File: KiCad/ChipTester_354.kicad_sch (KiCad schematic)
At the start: 3 parts

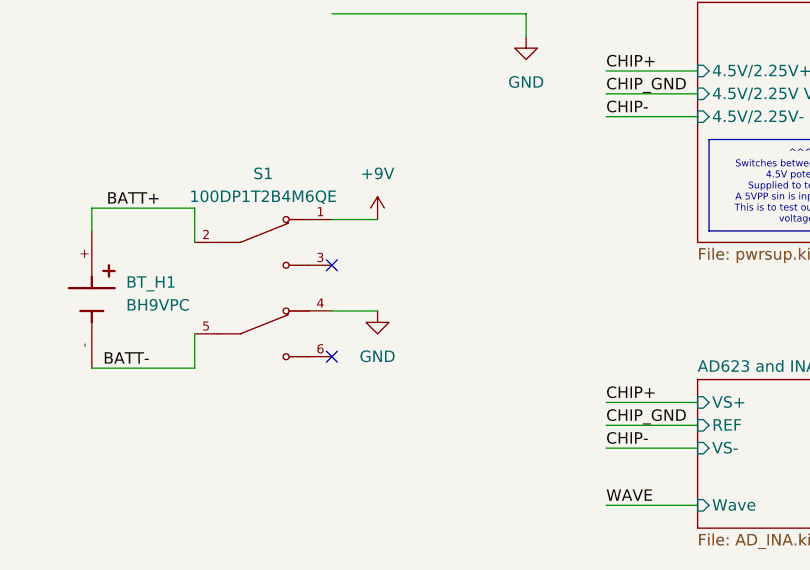
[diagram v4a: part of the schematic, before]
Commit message: Add power led
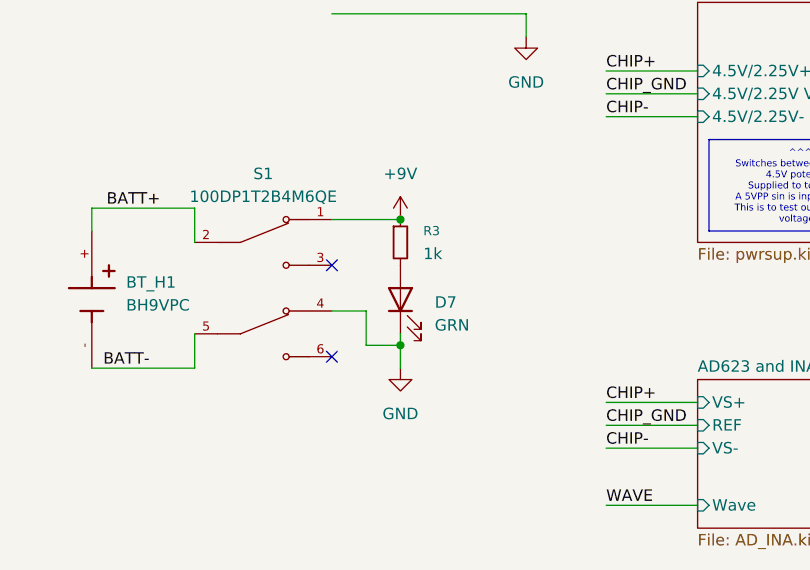
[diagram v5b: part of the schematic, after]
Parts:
- added D7: GRN, symbol Device:LED
- added R3: 1k, symbol Device:R_Small
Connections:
- net +9V: now also R3.1
- net GND: now also D7.1 (K)
- new net: D7.2 (A), R3.2
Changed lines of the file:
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@@
+	)
+	(junction
+		(at 111.76 54.61)
+		(diameter 0)
+		(color 0 0 0 0)
 	)
 	(junction
@@
 		(color 0 0 0 0)
 	)
+	(junction
+		(at 111.76 68.58)
+		(diameter 0)
+		(color 0 0 0 0)
+	)
 	(no_connect
 		(at 104.14 59.69)
@@
 	(wire
 		(pts
+			(xy 107.95 64.77) (xy 107.95 68.58)
+		)
+		(stroke
+			(width 0)
+			(type default)
+		)
+	)
+	(wire
+		(pts
 			(xy 217.17 40.64) (xy 227.33 40.64)
 		)
@@
 	(wire
 		(pts
+			(xy 111.76 68.58) (xy 111.76 67.31)
+		)
+		(stroke
+			(width 0)
+			(type default)
+		)
+	)
+	(wire
+		(pts
 			(xy 134.62 38.1) (xy 144.78 38.1)
 		)
@@
 	(wire
 		(pts
-			(xy 104.14 54.61) (xy 109.22 54.61)
-		)
-		(stroke
-			(width 0)
-			(type default)
-		)
-	)
-	(wire
-		(pts
 			(xy 134.62 80.01) (xy 144.78 80.01)
 		)
@@
 	(wire
 		(pts
-			(xy 109.22 64.77) (xy 104.14 64.77)
+			(xy 104.14 54.61) (xy 111.76 54.61)
 		)
 		(stroke
@@
 	(wire
 		(pts
+			(xy 104.14 64.77) (xy 107.95 64.77)
+		)
+		(stroke
+			(width 0)
+			(type default)
+		)
+	)
+	(wire
+		(pts
 			(xy 134.62 77.47) (xy 144.78 77.47)
 		)
@@
 		(pts
 			(xy 77.47 53.34) (xy 77.47 55.88)
+		)
+		(stroke
+			(width 0)
+			(type default)
+		)
+	)
+	(wire
+		(pts
+			(xy 107.95 68.58) (xy 111.76 68.58)
+		)
+		(stroke
+			(width 0)
+			(type default)
+		)
+	)
+	(wire
+		(pts
+			(xy 111.76 68.58) (xy 111.76 71.12)
 		)
 		(stroke
@@
 	(symbol
 		(lib_id "power:+9V")
-		(at 109.22 54.61 0)
+		(at 111.76 54.61 0)
 		(unit 1)
 		(exclude_from_sim no)
@@
 		(fields_autoplaced yes)
 		(property "Reference" "#PWR02"
-			(at 109.22 58.42 0)
+			(at 111.76 58.42 0)
 			(effects
 				(font
@@
 		)
 		(property "Value" "+9V"
-			(at 109.22 49.53 0)
+			(at 111.76 49.53 0)
 			(effects
 				(font
@@
 		)
 		(property "Footprint" ""
-			(at 109.22 54.61 0)
+			(at 111.76 54.61 0)
 			(effects
 				(font
@@
 		)
 		(property "Datasheet" ""
-			(at 109.22 54.61 0)
+			(at 111.76 54.61 0)
 			(effects
 				(font
@@
 		)
 		(property "Description" "Power symbol creates a global label with name \"+9V\""
-			(at 109.22 54.61 0)
+			(at 111.76 54.61 0)
 			(effects
 				(font
@@
 	)
 	(symbol
+		(lib_id "Device:LED")
+		(at 111.76 63.5 90)
+		(unit 1)
+		(exclude_from_sim no)
+		(in_bom yes)
+		(on_board yes)
+		(dnp no)
+		(fields_autoplaced yes)
+		(property "Reference" "D7"
+			(at 115.57 63.8174 90)
+			(effects
+				(font
+					(size 1.27 1.27)
+				)
+				(justify right)
+			)
+		)
+		(property "Value" "GRN"
+			(at 115.57 66.3574 90)
+			(effects
+				(font
+					(size 1.27 1.27)
+				)
+				(justify right)
+			)
+		)
+		(property "Footprint" ""
+			(at 111.76 63.5 0)
+			(effects
+				(font
+					(size 1.27 1.27)
+				)
+				(hide yes)
+			)
+		)
+		(property "Datasheet" "~"
+			(at 111.76 63.5 0)
+			(effects
+				(font
+					(size 1.27 1.27)
+				)
+				(hide yes)
+			)
+		)
+		(property "Description" "Light emitting diode"
+			(at 111.76 63.5 0)
+			(effects
+				(font
+					(size 1.27 1.27)
+				)
+				(hide yes)
+			)
+		)
+		(property "Sim.Pins" "1=K 2=A"
+			(at 111.76 63.5 0)
+			(effects
+				(font
+					(size 1.27 1.27)
+				)
+				(hide yes)
+			)
+		)
+		(pin "2"
+		)
+		(pin "1"
+		)
+		(instances
+			(project ""
+				(path "/57b9e980-cd8f-44e4-af61-2cbd5bb30325"
+					(reference "D7")
+					(unit 1)
+				)
+			)
+		)
+	)
+	(symbol
 		(lib_id "power:GND")
 		(at 194.31 46.99 0)
@@
 	(symbol
 		(lib_id "power:GND")
-		(at 109.22 64.77 0)
+		(at 111.76 71.12 0)
 		(unit 1)
 		(exclude_from_sim no)
@@
 		(fields_autoplaced yes)
 		(property "Reference" "#PWR010"
-			(at 109.22 71.12 0)
+			(at 111.76 77.47 0)
 			(effects
 				(font
@@
 		)
 		(property "Value" "GND"
-			(at 109.22 69.85 0)
+			(at 111.76 76.2 0)
 			(effects
 				(font
@@
 		)
 		(property "Footprint" ""
-			(at 109.22 64.77 0)
+			(at 111.76 71.12 0)
 			(effects
 				(font
@@
 		)
 		(property "Datasheet" ""
-			(at 109.22 64.77 0)
+			(at 111.76 71.12 0)
 			(effects
 				(font
@@
 		)
 		(property "Description" "Power symbol creates a global label with name \"GND\" , ground"
-			(at 109.22 64.77 0)
+			(at 111.76 71.12 0)
 			(effects
 				(font
@@
 					(unit 1)
 				)
+			)
+		)
+	)
+	(symbol
+		(lib_id "Device:R_Small")
+		(at 111.76 57.15 0)
+		(unit 1)
+		(exclude_from_sim no)
+		(in_bom yes)
+		(on_board yes)
+		(dnp no)
+		(fields_autoplaced yes)
+		(property "Reference" "R3"
+			(at 114.3 55.8799 0)
+			(effects
+				(font
+					(size 1.016 1.016)
+				)
+				(justify left)
+			)
+		)
+		(property "Value" "1k"
+			(at 114.3 58.4199 0)
+			(effects
+				(font
+					(size 1.27 1.27)
+				)
+				(justify left)
+			)
+		)
+		(property "Footprint" ""
+			(at 111.76 57.15 0)
+			(effects
+				(font
+					(size 1.27 1.27)
+				)
+				(hide yes)
+			)
+		)
+		(property "Datasheet" "~"
+			(at 111.76 57.15 0)
+			(effects
+				(font
+					(size 1.27 1.27)
+				)
+				(hide yes)
+			)
+		)
+		(property "Description" "Resistor, small symbol"
+			(at 111.76 57.15 0)
+			(effects
+				(font
+					(size 1.27 1.27)
+				)
+				(hide yes)
+			)
+		)
+		(pin "1"
+		)
+		(pin "2"
+		)
+		(instances
+			(project ""
+				(path "/57b9e980-cd8f-44e4-af61-2cbd5bb30325"
+					(reference "R3")
+					(unit 1)
+				)

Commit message: updated footprint to be all THT, battery holder still not there
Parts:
- D7: footprint (none) -> Diode_THT:D_5W_P5.08mm_Vertical_AnodeUp
- R3: footprint (none) -> Resistor_THT:R_Axial_DIN0204_L3.6mm_D1.6mm_P2.54mm_Vertical
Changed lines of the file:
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@@
 			)
 		)
-		(property "Footprint" ""
+		(property "Footprint" "Diode_THT:D_5W_P5.08mm_Vertical_AnodeUp"
 			(at 111.76 63.5 0)
 			(effects
@@
 			)
 		)
-		(property "Footprint" ""
+		(property "Footprint" "Resistor_THT:R_Axial_DIN0204_L3.6mm_D1.6mm_P2.54mm_Vertical"
 			(at 111.76 57.15 0)
 			(effects

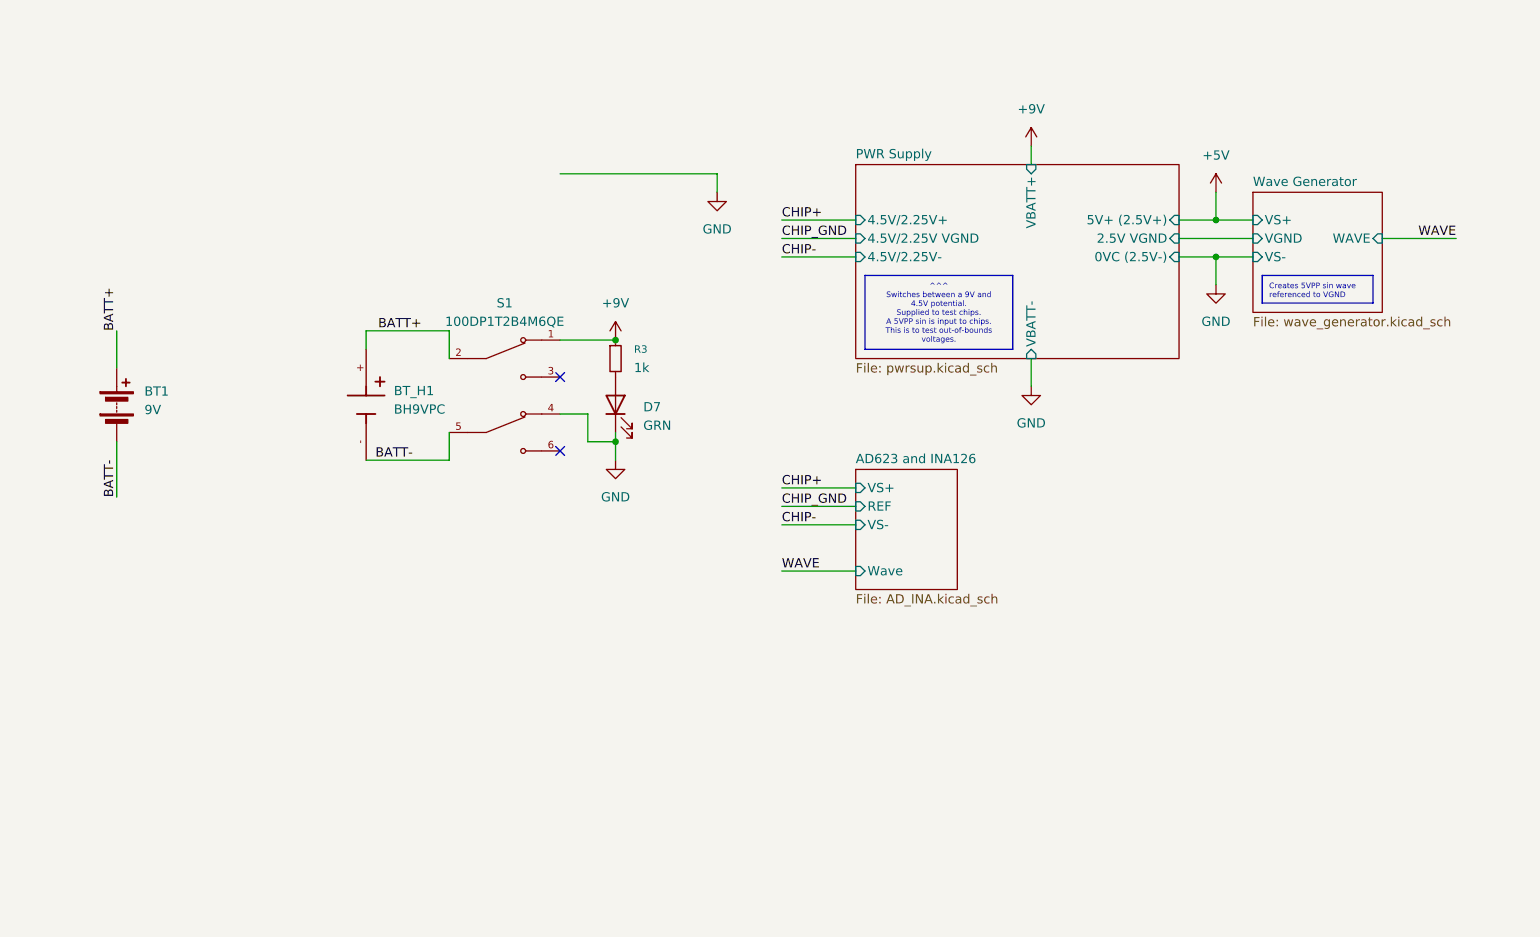
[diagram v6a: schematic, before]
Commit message: Some TP -> Headers, added footprints, fixed battery footprint, started layout of board.
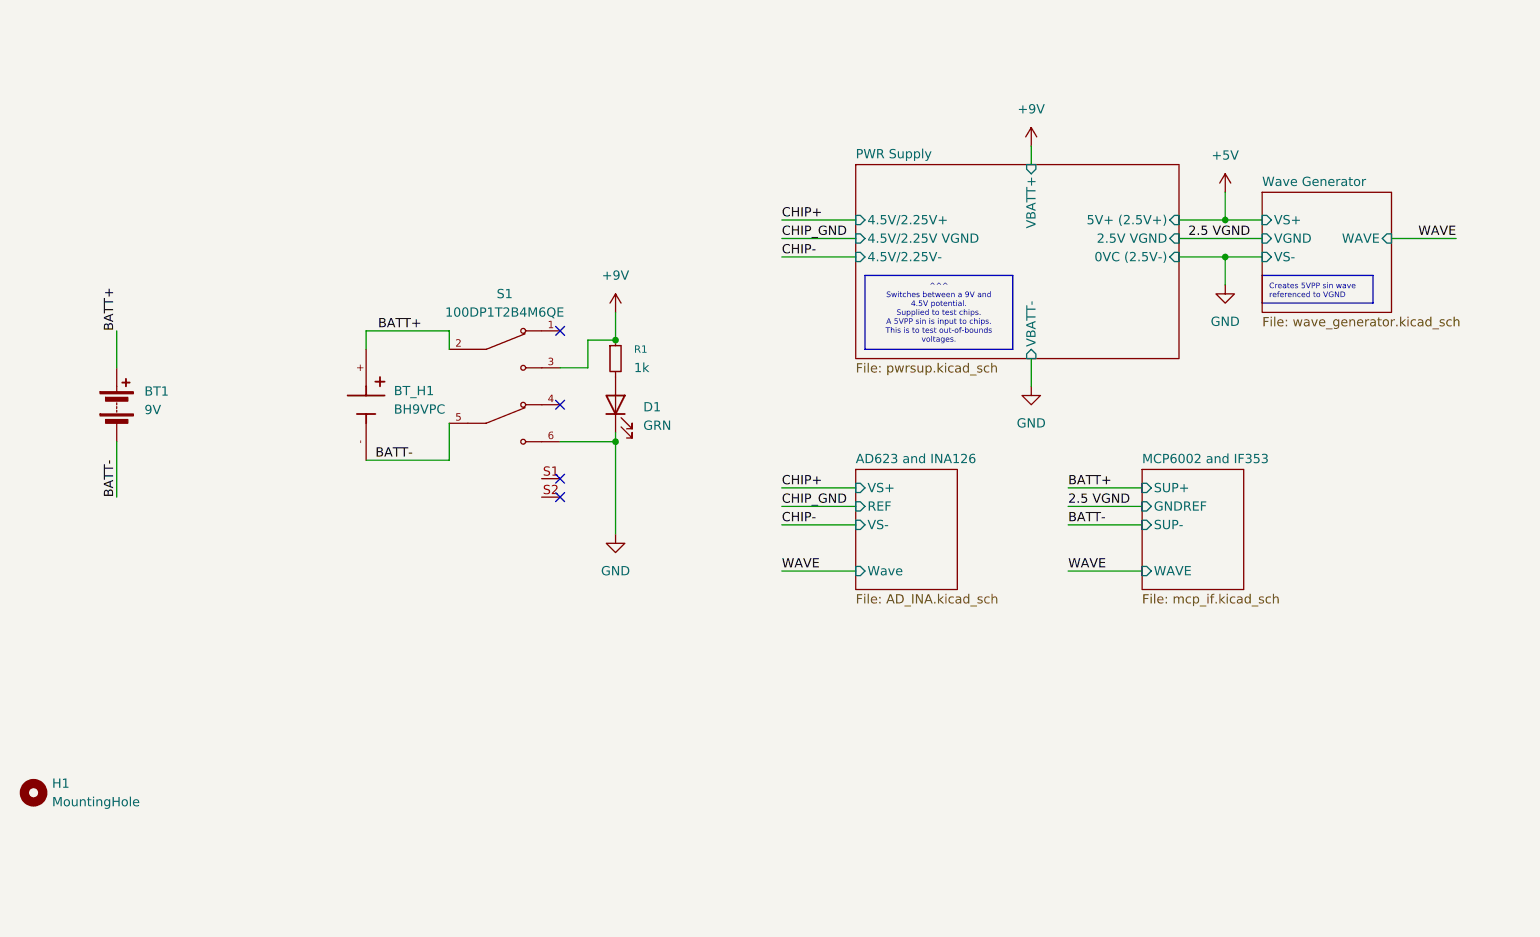
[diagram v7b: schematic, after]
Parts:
- added H1: MountingHole, MountingHole:MountingHole_3.2mm_M3, symbol Mechanical:MountingHole
- renumbered D7 to D1, R3 to R1
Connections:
- net +9V: now also S1.3; no longer S1.1
- net GND: now also S1.6; no longer S1.4
- no-connect marks 2 -> 4
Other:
- added sheet MCP6002 and IF353 (mcp_if.kicad_sch)

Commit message: Made the board :D
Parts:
- added H2, H3, H4: MountingHole, MountingHole:MountingHole_3.2mm_M3, symbol Mechanical:MountingHole
- D1: footprint Diode_THT:D_5W_P5.08mm_Vertical_AnodeUp -> LED_THT:LED_D5.0mm
- R1: footprint Resistor_THT:R_Axial_DIN0204_L3.6mm_D1.6mm_P2.54mm_Vertical -> Resistor_THT:R_Axial_DIN0207_L6.3mm_D2.5mm_P7.62mm_Horizontal
